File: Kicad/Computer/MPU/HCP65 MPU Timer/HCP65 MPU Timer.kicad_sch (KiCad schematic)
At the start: 20 parts, among them IC1 74LVC2G74DP,125, IC11 74LVC1G27GW,125, IC14 74HCT4040PW,118, IC2 74LVC273PW,118, IC5 AP7365-33WG-7, IC6 74HCT4040PW,118, IC7 PI3B3251QE, IC9 74LVC541APW,118, J1 Pin_Header_01x16, J2 Conn_02x16_Counter_Clockwise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

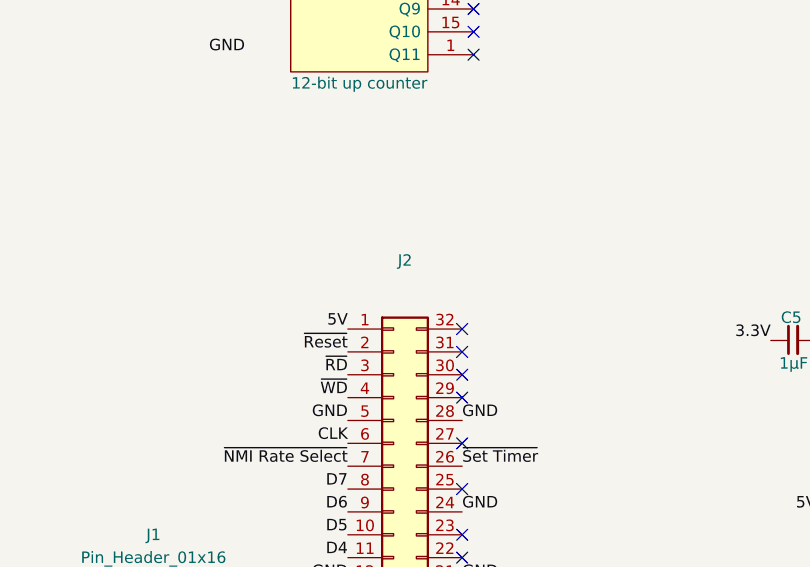
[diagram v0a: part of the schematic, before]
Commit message: Cleaned up Processor Board traces and grounding.
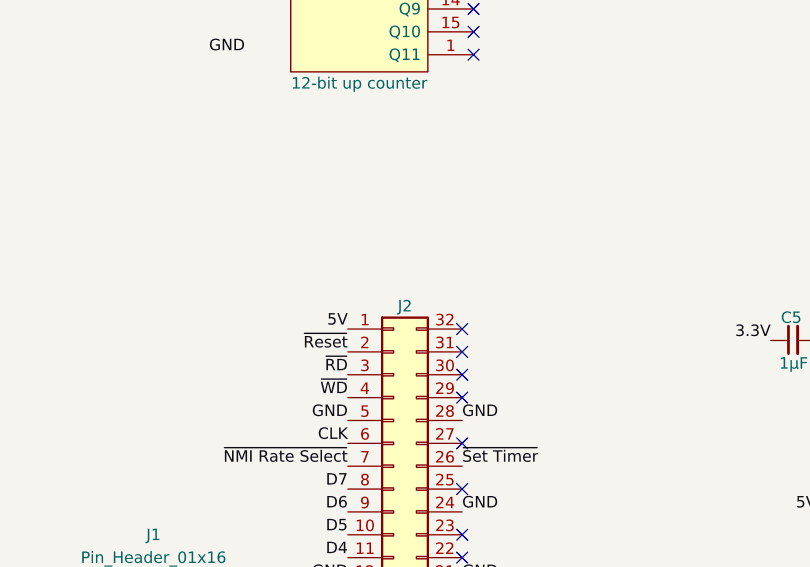
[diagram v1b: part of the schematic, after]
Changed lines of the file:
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@@
   (symbol (lib_id "Connector_Generic:Conn_02x16_Counter_Clockwise") (at 57.15 144.78 0) (unit 1)
     (in_bom yes) (on_board yes) (dnp no)
-    (property "Reference" "J2" (at 58.42 119.38 0)
+    (property "Reference" "J2" (at 58.42 124.46 0)
       (effects (font (size 1.27 1.27)))
     )

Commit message: Generating MPU gerbers again with paste layers.
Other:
- moved on the sheet: C10, C11, C15, C16, C5, C6, C7, C8, C9, IC1, IC11, IC14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

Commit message: Re-autorouted a bunch of boards.  Or something.  I don't know.
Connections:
- net D0: now also J2.8 (Pin_8); no longer J2.16 (Pin_16)
- net D1: now also J2.9 (Pin_9); no longer J2.15 (Pin_15)
- net D2: now also J2.10 (Pin_10); no longer J2.14 (Pin_14)
- net D3: now also J2.11 (Pin_11); no longer J2.13 (Pin_13)
- net D4: now also J2.13 (Pin_13); no longer J2.11 (Pin_11)
- net D5: now also J2.14 (Pin_14); no longer J2.10 (Pin_10)
- net D6: now also J2.15 (Pin_15); no longer J2.9 (Pin_9)
- net D7: now also J2.16 (Pin_16); no longer J2.8 (Pin_8)
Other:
- moved on the sheet: C10, C11, C15, C16, C5, C6, C7, C8, C9, IC1, IC11, IC14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

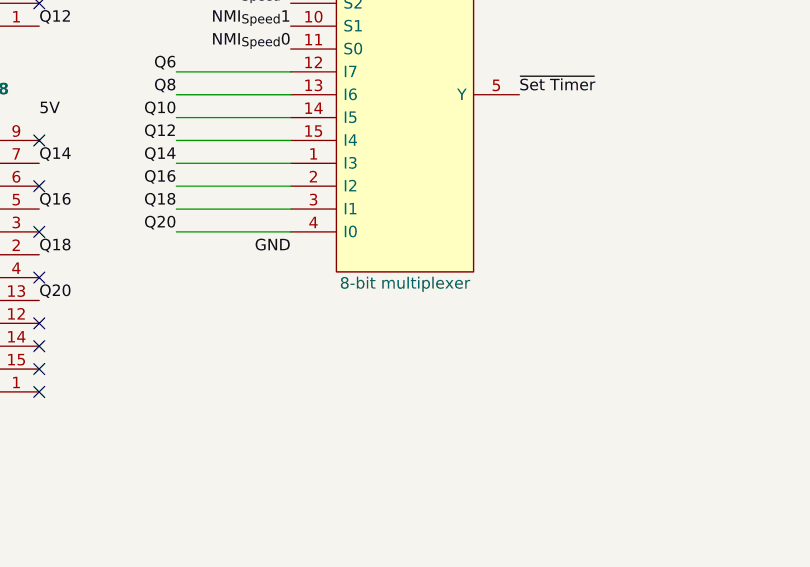
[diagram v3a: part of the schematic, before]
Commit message: Manually re-routing the Small Mainboard.
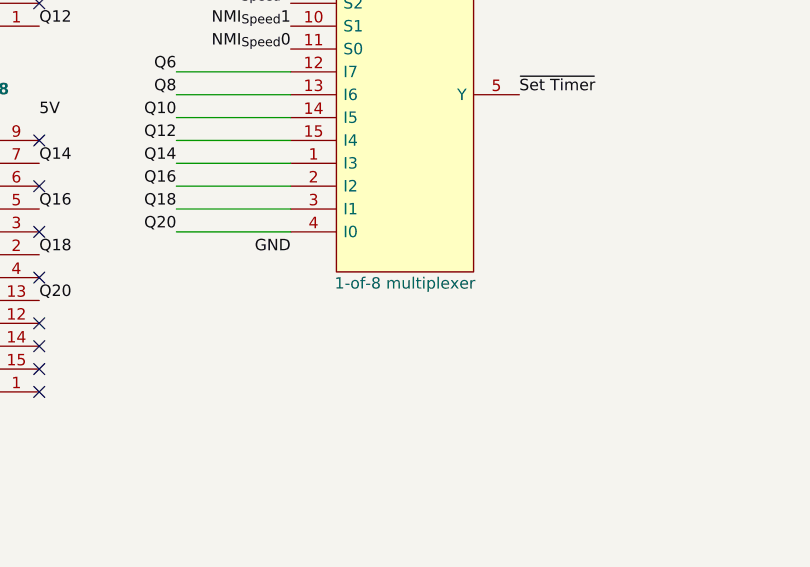
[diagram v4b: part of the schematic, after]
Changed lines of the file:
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@@
       (effects (font (size 1.27 1.27)) (justify left) hide)
     )
-    (property "Description" "8-bit multiplexer" (at 153.67 104.775 0)
+    (property "Description" "1-of-8 multiplexer" (at 153.67 104.775 0)
       (effects (font (size 1.27 1.27)))
     )

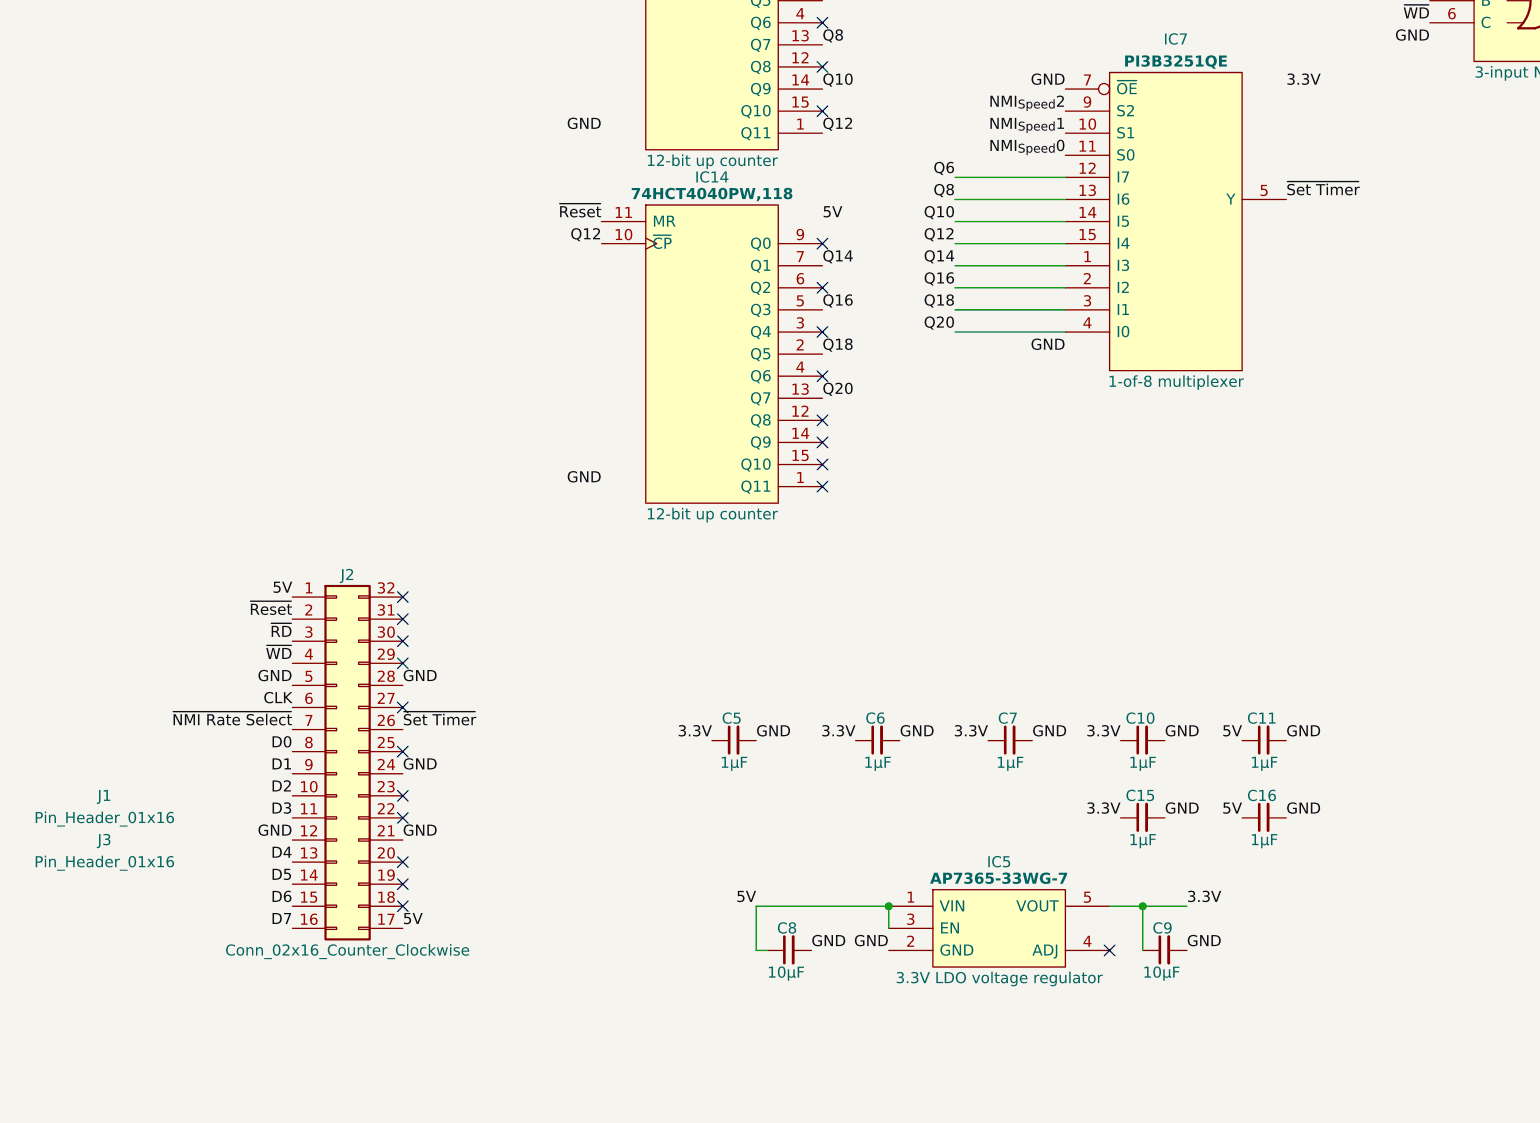
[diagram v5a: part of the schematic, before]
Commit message: Converted more PCBs to Kicad 8.
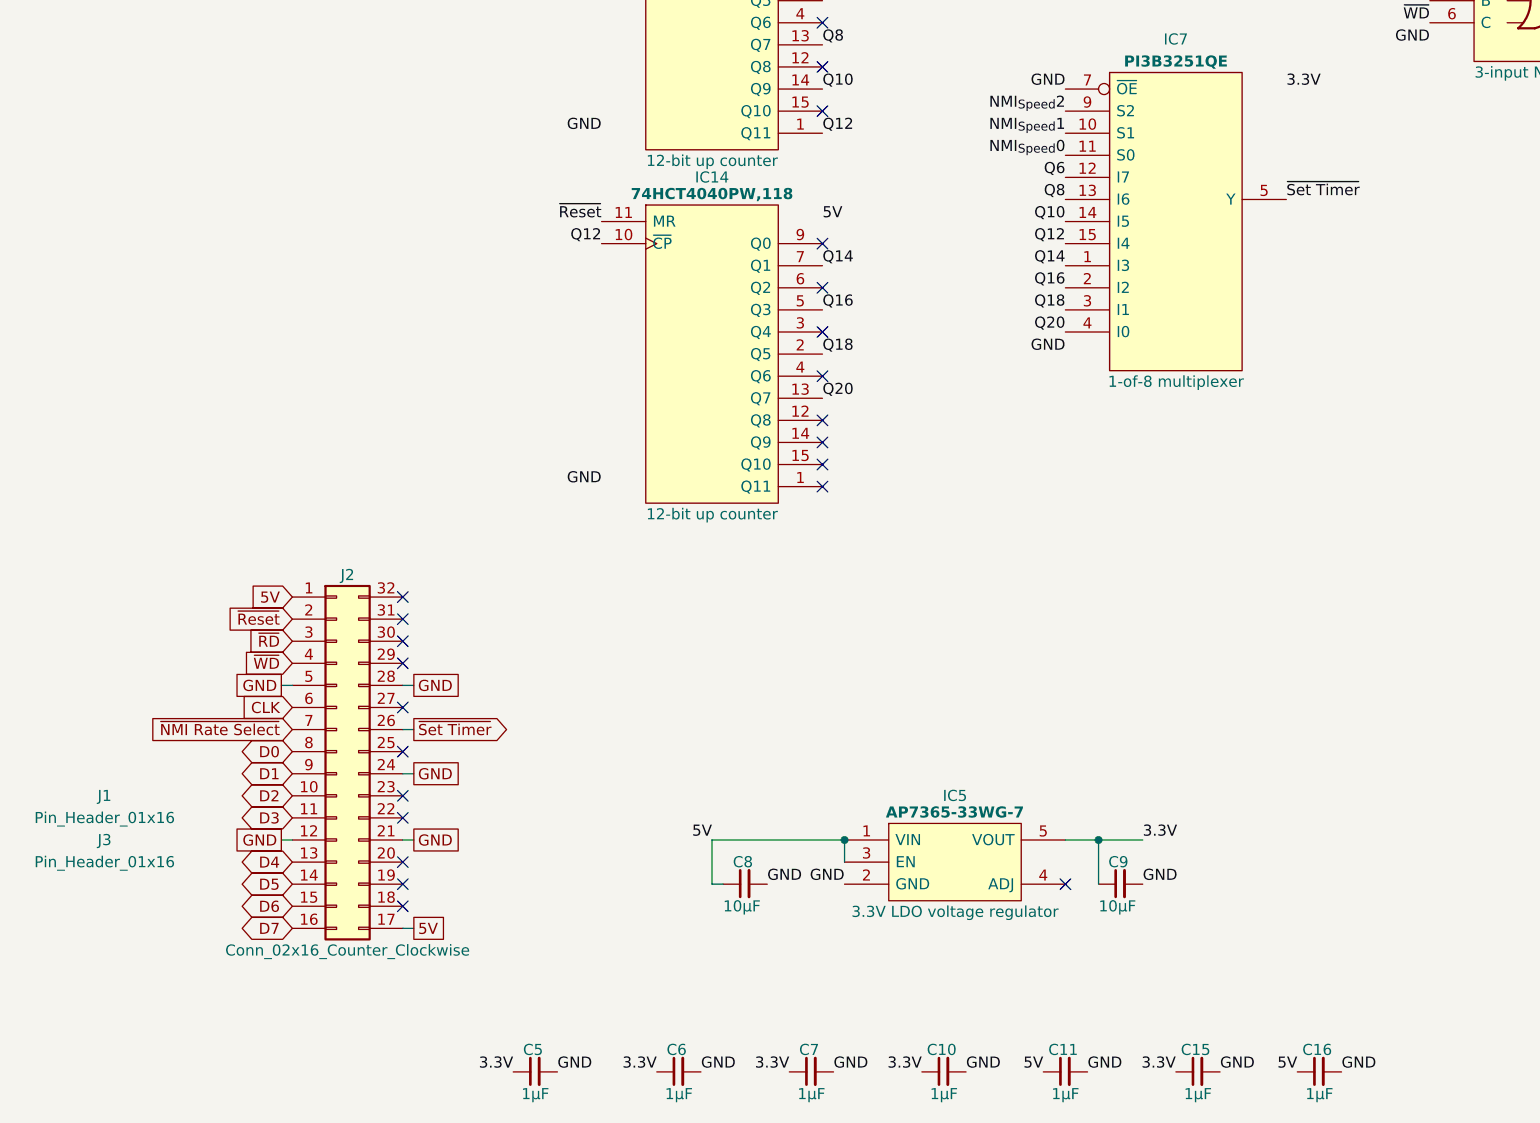
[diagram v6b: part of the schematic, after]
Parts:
- C10, C11, C15, C16, C5, C6, C7, C8, C9: Garbage (none) -> Unpolarized capacitor, small symbol
- IC1: footprint SOP65P400X110-8N -> SamacSys_Parts:SOP65P400X110-8N; Garbage (none) -> 74LVC2G74 - Single D-type flip-flop with set and reset; pos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
- IC11: footprint SOP65P210X110-6N -> SamacSys_Parts:SOP65P210X110-6N; Garbage (none) -> 74LVC1G27 - Single 3-input NOR gate@en-us
- IC14, IC6: footprint SOP65P640X110-16N -> SamacSys_Parts:SOP65P640X110-16N; Garbage (none) -> 74HC(T)4040 - 12-stage binary ripple counter@en-us
- IC2: footprint SOP65P640X110-20N -> SamacSys_Parts:SOP65P640X110-20N; Garbage (none) -> Nexperia 74LVC273PW,118 D Type Flip Flop IC, D Type Flip-Fl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
- IC5: footprint SOT95P285X130-5N -> SamacSys_Parts:SOT95P285X130-5N; Garbage (none) -> DiodesZetex AP7365-33WG-7, LDO Voltage Regulator, 600mA, 3.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
- IC7: footprint SOP64P599X175-16N -> SamacSys_Parts:SOP64P599X175-16N; Garbage (none) -> Encoders, Decoders, Multiplexers & Demultiplexers 3.3V 8:1 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
- IC9: footprint SOP65P640X110-20N -> SamacSys_Parts:SOP65P640X110-20N; Garbage (none) -> 74LVC541A - Octal buffer/line driver with 5 V tolerant inpu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
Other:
- moved on the sheet: C10, C11, C15, C16, C5, C6, C7, C8, C9, IC5
